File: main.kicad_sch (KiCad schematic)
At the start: 0 parts

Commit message: feat: started power supply and created lib folder
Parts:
- added J1: USB_C_Receptacle, symbol Connector:USB_C_Receptacle
- added J2: B2B-XH-A, B2B-XH-A:JST_B2B-XH-A, symbol B2B-XH-A:B2B-XH-A
- added R1, R2: 5.5k, symbol Device:R
- added U1: ~, symbol Power_LDO_TexasInstruments:TLV740P
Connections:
- new net: J1.A5 (CC1), R2.1
- new net: J1.B5 (CC2), R1.1
- new net +3V3: U1.3 (OUT)
- new net GND: J1.A1 (GND), J1.A12 (GND), J1.B1 (GND), J1.B12 (GND), R1.2, R2.2, U1.4 (GND)
- new net VBUS: J1.A4 (VBUS), J1.A9 (VBUS), J1.B4 (VBUS), J1.B9 (VBUS), U1.1 (IN), U1.2 (EN)
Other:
- note added: "LDO"
- note added: "USB-C"

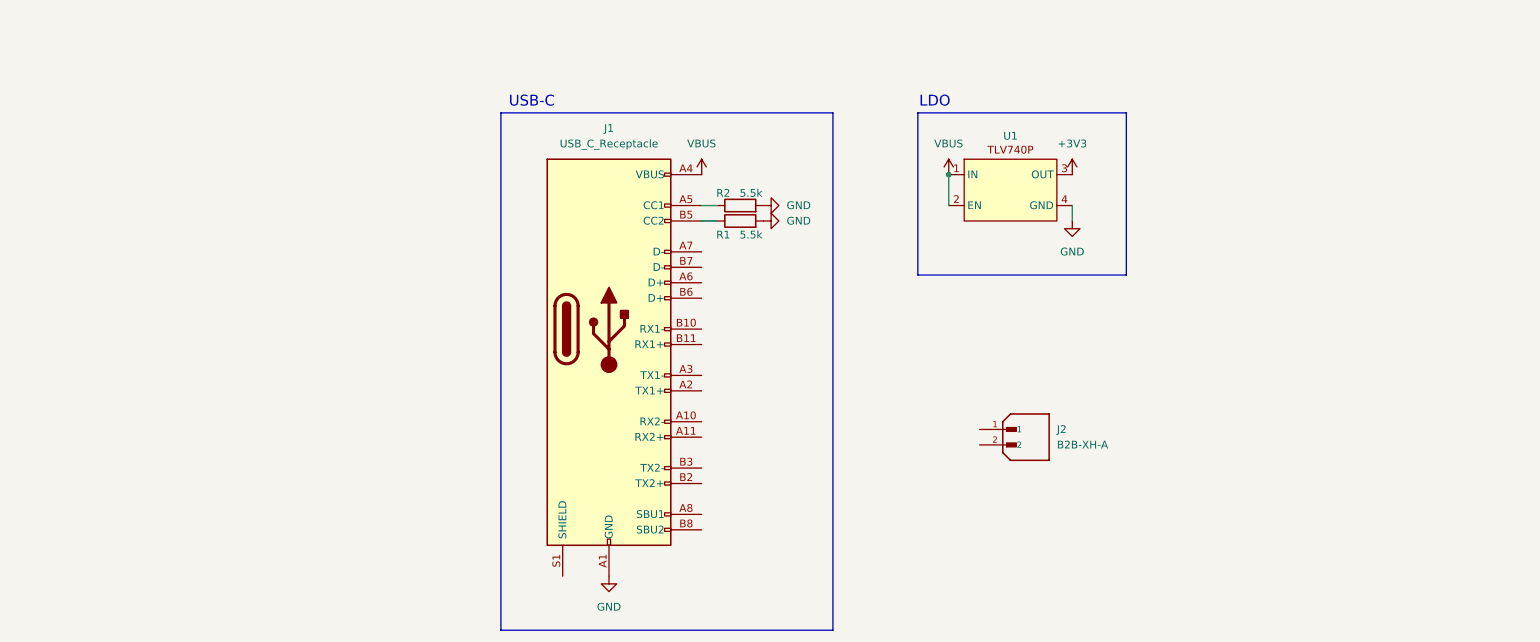
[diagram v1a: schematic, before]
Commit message: Feat: added more things to the power supply
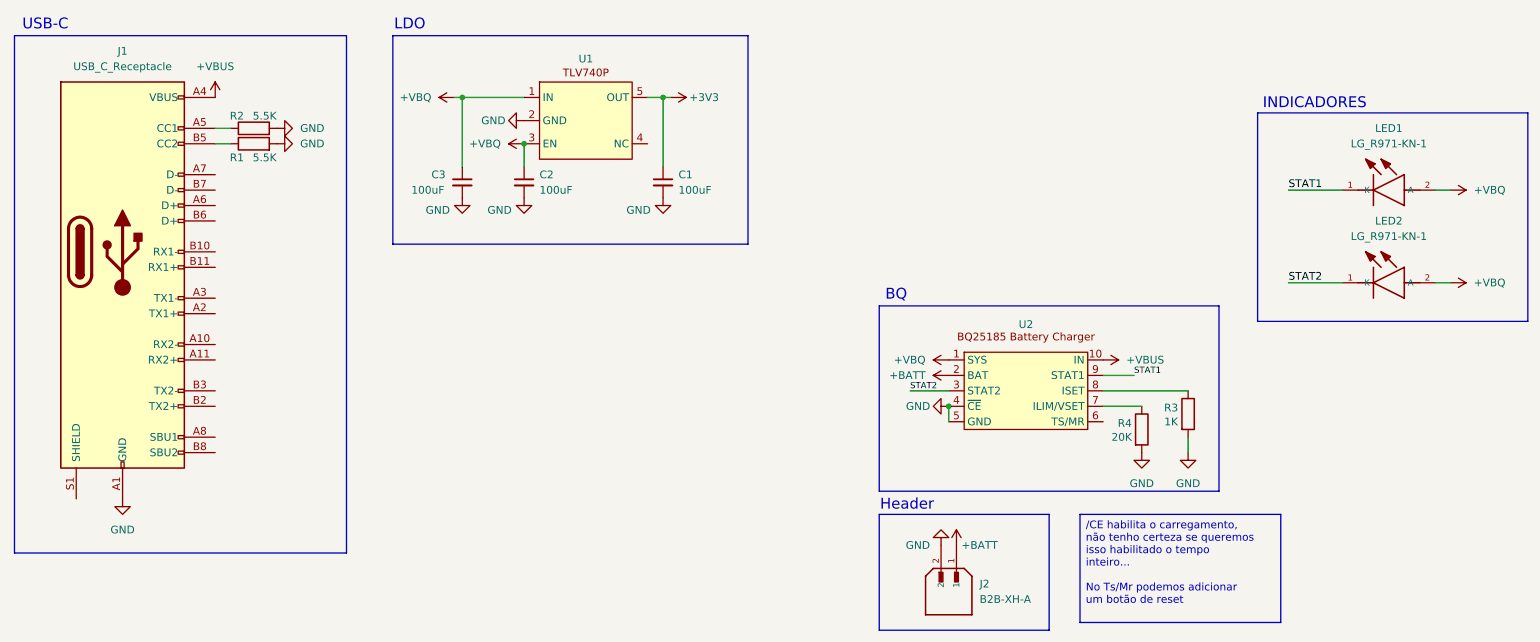
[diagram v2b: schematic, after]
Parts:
- added C1, C2, C3: 100uF, symbol Device:C_Small
- added LED1, LED2: LG_R971-KN-1, LG_R971-KN-1:LEDC2012X80N, symbol LG_R971-KN-1:LG_R971-KN-1
- added R3: 1K, symbol Device:R
- added R4: 20K, symbol Device:R
- added U2: ~, symbol Power_PMIC_TexasInstruments_BQ25185:BQ25185DLHR
- R1, R2: value 5.5k -> 5.5K
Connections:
- net +3V3: now also U1.5 (OUT), C1.1; no longer U1.3 (OUT)
- net GND: now also J2.2, U1.2 (GND), C1.2, C2.2, C3.2, R3.2, R4.2, U2.4 (~{CE}), U2.5 (GND); no longer U1.4 (GND)
- net +BATT: now reaches J2.1
- net +BATT: now also U2.2 (BAT)
- net VBUS renamed +VBUS
- net +VBUS: now also U2.10 (IN); no longer U1.1 (IN), U1.2 (EN)
- new net: R4.1, U2.7 (ILIM/VSET)
- new net: R3.1, U2.8 (ISET)
- new net +VBQ: C2.1, C3.1, LED1.2 (A), LED2.2 (A), U1.1 (IN), U1.3 (EN), U2.1 (SYS)
- new net STAT1: LED1.1 (K), U2.9 (STAT1)
- new net STAT2: LED2.1 (K), U2.3 (STAT2)
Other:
- note added: "BQ"
- note added: "Header"
- note added: "INDICADORES"
- company: (none) -> Os Circuitados
- title: (none) -> Power Supply
- moved on the sheet: J1, J2, R1, R2

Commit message: feat: added MPN to resistors, changed USB_C receptacle
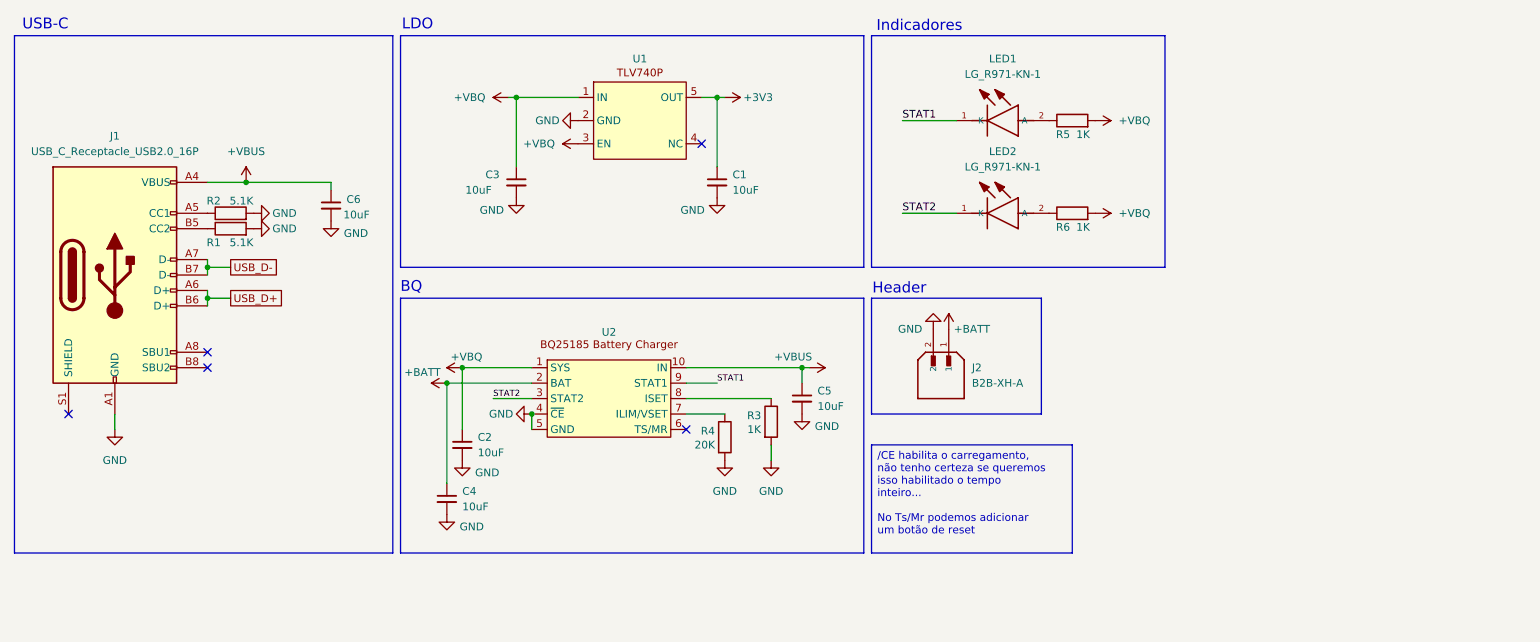
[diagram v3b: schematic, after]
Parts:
- removed J1: USB_C_Receptacle, symbol Connector:USB_C_Receptacle
- added C4, C5, C6: 10uF, symbol Device:C_Small
- added J1: USB_C_Receptacle_USB2.0_16P, symbol Connector:USB_C_Receptacle_USB2.0_16P
- added R5, R6: 1K, symbol Device:R
- C1, C2, C3: value 100uF -> 10uF
- R1, R2: value 5.5K -> 5.1K; MPN (none) -> AC0402FR-075K1L
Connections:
- net +BATT: now also C4.1
- net +VBQ: now also R5.2, R6.2; no longer LED1.2 (A), LED2.2 (A)
- net +VBUS: now also C5.1, C6.1, J1.A4 (VBUS), J1.A9 (VBUS), J1.B4 (VBUS), J1.B9 (VBUS)
- net GND: now also C4.2, C5.2, C6.2, J1.A1 (GND), J1.A12 (GND), J1.B1 (GND), J1.B12 (GND)
- net at R2.1: now also J1.A5 (CC1)
- net at R1.1: now also J1.B5 (CC2)
- new net: LED1.2 (A), R5.1
- new net: LED2.2 (A), R6.1
- new net USB_D+: J1.A6 (D+), J1.B6 (D+)
- new net USB_D-: J1.A7 (D-), J1.B7 (D-)
- no-connect marks 0 -> 5
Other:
- note added: "Indicadores"
- note removed: "INDICADORES"
- moved on the sheet: C1, C3, J2, LED1, LED2, R1, R2, R3, R4, U1, U2

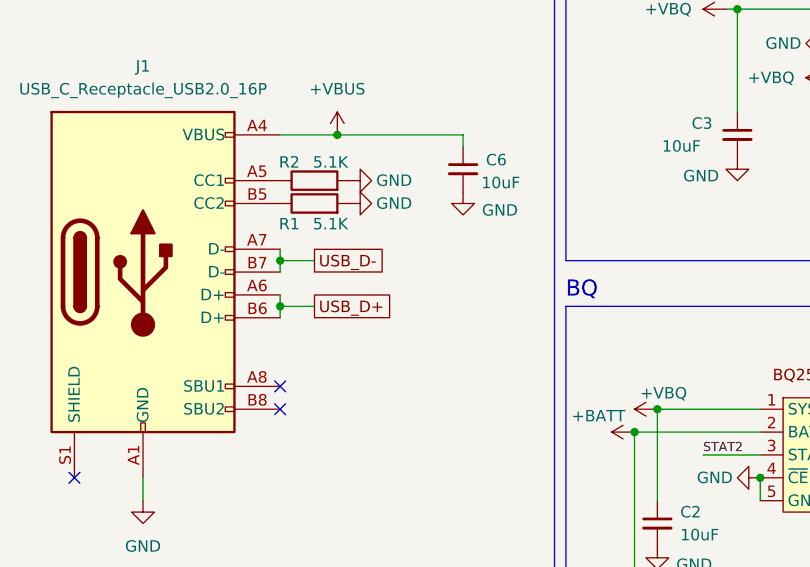
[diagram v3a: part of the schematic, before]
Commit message: refac: changed USB_D+ and USB_D-
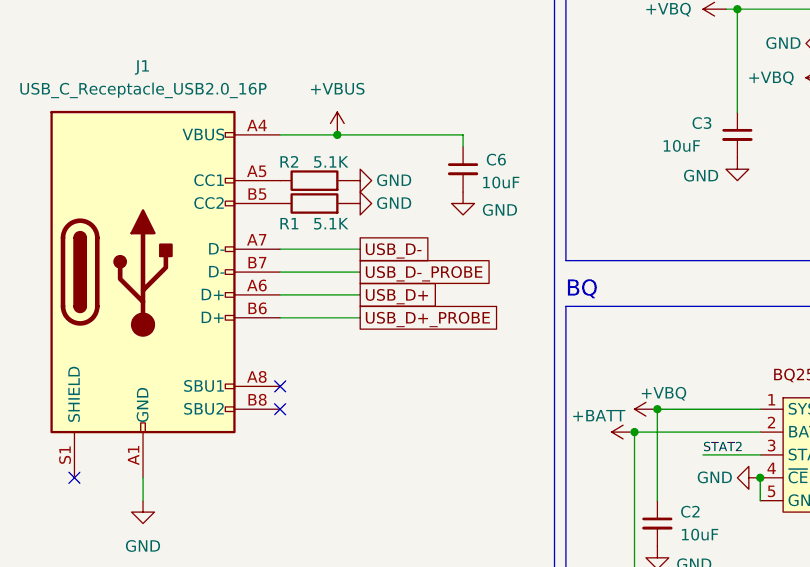
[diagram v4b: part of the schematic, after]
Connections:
- net USB_D+: no longer J1.B6 (D+)
- net USB_D-: no longer J1.B7 (D-)
- new net USB_D+_PROBE: J1.B6 (D+)
- new net USB_D-_PROBE: J1.B7 (D-)
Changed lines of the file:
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@@
-	)
-	(junction
-		(at 53.34 78.74)
-		(diameter 0)
-		(color 0 0 0 0)
-	)
-	(junction
-		(at 53.34 73.66)
-		(diameter 0)
-		(color 0 0 0 0)
 	)
 	(junction
@@
 	(wire
 		(pts
-			(xy 53.34 72.39) (xy 53.34 73.66)
+			(xy 53.34 80.01) (xy 62.23 80.01)
 		)
 		(stroke
@@
 	(wire
 		(pts
+			(xy 53.34 74.93) (xy 62.23 74.93)
+		)
+		(stroke
+			(width 0)
+			(type default)
+		)
+	)
+	(wire
+		(pts
+			(xy 53.34 77.47) (xy 62.23 77.47)
+		)
+		(stroke
+			(width 0)
+			(type default)
+		)
+	)
+	(wire
+		(pts
 			(xy 104.14 45.72) (xy 104.14 57.15)
 		)
@@
 	(wire
 		(pts
-			(xy 53.34 73.66) (xy 57.15 73.66)
-		)
-		(stroke
-			(width 0)
-			(type default)
-		)
-	)
-	(wire
-		(pts
 			(xy 73.66 59.69) (xy 59.69 59.69)
 		)
@@
 	(wire
 		(pts
-			(xy 53.34 77.47) (xy 53.34 78.74)
-		)
-		(stroke
-			(width 0)
-			(type default)
-		)
-	)
-	(wire
-		(pts
 			(xy 167.64 64.77) (xy 176.53 64.77)
 		)
@@
 	(wire
 		(pts
-			(xy 53.34 73.66) (xy 53.34 74.93)
-		)
-		(stroke
-			(width 0)
-			(type default)
-		)
-	)
-	(wire
-		(pts
 			(xy 167.64 49.53) (xy 176.53 49.53)
 		)
@@
 	(wire
 		(pts
-			(xy 53.34 78.74) (xy 57.15 78.74)
-		)
-		(stroke
-			(width 0)
-			(type default)
-		)
-	)
-	(wire
-		(pts
 			(xy 53.34 59.69) (xy 59.69 59.69)
 		)
@@
 	(wire
 		(pts
-			(xy 53.34 78.74) (xy 53.34 80.01)
+			(xy 53.34 72.39) (xy 62.23 72.39)
 		)
 		(stroke
@@
 		)
 	)
-	(global_label "USB_D-"
+	(global_label "USB_D+_PROBE"
 		(shape passive)
-		(at 57.15 73.66 0)
+		(at 62.23 80.01 0)
 		(fields_autoplaced yes)
 		(effects
@@
 		)
 		(property "Intersheetrefs" "${INTERSHEET_REFS}"
-			(at 66.6439 73.66 0)
+			(at 78.981 80.01 0)
 			(effects
 				(font
@@
 		)
 	)
+	(global_label "USB_D-_PROBE"
+		(shape passive)
+		(at 62.23 74.93 0)
+		(fields_autoplaced yes)
+		(effects
+			(font
+				(size 1.27 1.27)
+			)
+			(justify left)
+		)
+		(property "Intersheetrefs" "${INTERSHEET_REFS}"
+			(at 78.981 74.93 0)
+			(effects
+				(font
+					(size 1.27 1.27)
+				)
+				(justify left)
+				(hide yes)
+			)
+		)
+	)
+	(global_label "USB_D-"
+		(shape passive)
+		(at 62.23 72.39 0)
+		(fields_autoplaced yes)
+		(effects
+			(font
+				(size 1.27 1.27)
+			)
+			(justify left)
+		)
+		(property "Intersheetrefs" "${INTERSHEET_REFS}"
+			(at 71.7239 72.39 0)
+			(effects
+				(font
+					(size 1.27 1.27)
+				)
+				(justify left)
+				(hide yes)
+			)
+		)
+	)
 	(global_label "USB_D+"
 		(shape passive)
-		(at 57.15 78.74 0)
+		(at 62.23 77.47 0)
 		(fields_autoplaced yes)
 		(effects
@@
 		)
 		(property "Intersheetrefs" "${INTERSHEET_REFS}"
-			(at 66.6439 78.74 0)
+			(at 71.7239 77.47 0)
 			(effects
 				(font
